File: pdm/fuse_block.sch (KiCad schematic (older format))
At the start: 15 parts, among them Q1 BC817, Q6 Q_NPN_BCE, U5 BTS443P

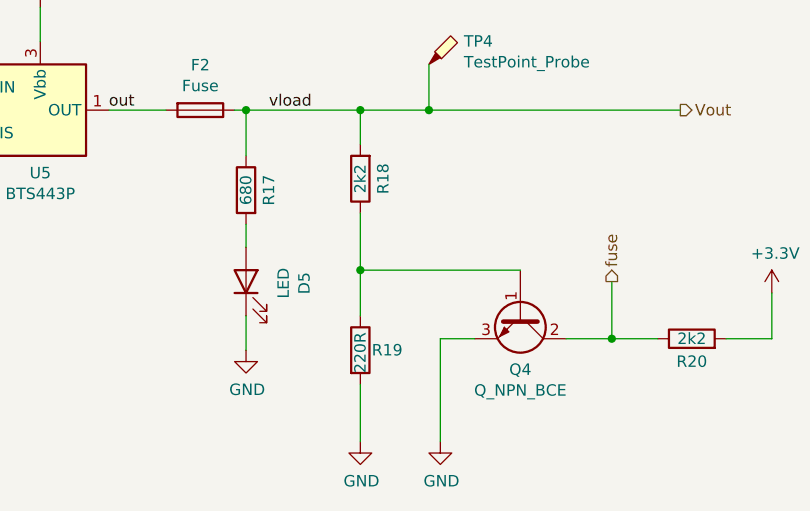
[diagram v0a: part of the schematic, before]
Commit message: added digikey BoM
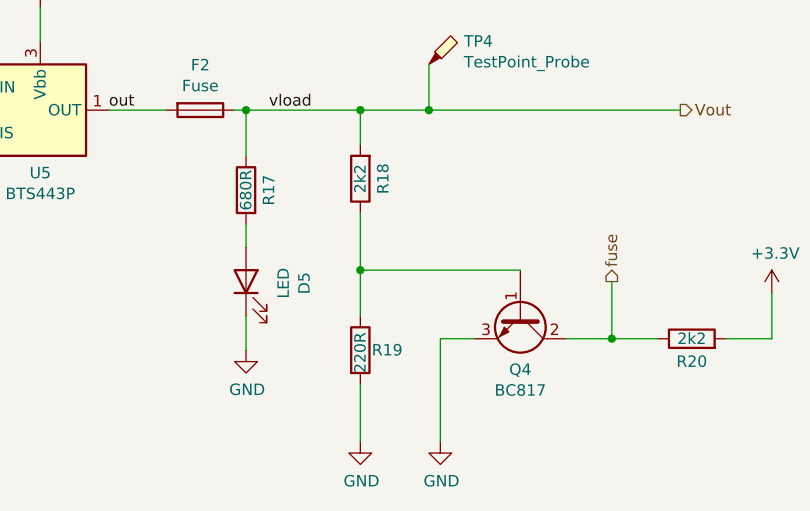
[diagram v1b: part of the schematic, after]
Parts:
- D5: Digi-Key_PN (none) -> 516-1431-1-ND
- Q1: Digi-Key_PN (none) -> 1727-6186-1-ND
- Q6: value Q_NPN_BCE -> BC817; Digi-Key_PN (none) -> 1727-6186-1-ND
- R16: Digi-Key_PN (none) -> A106057CT-ND
- R17: value 680 -> 680R; Digi-Key_PN (none) -> A129747CT-ND
- R18, R20: Digi-Key_PN (none) -> A106060CT-ND
- R19: Digi-Key_PN (none) -> 311-220CRCT-ND
- R21: Digi-Key_PN (none) -> 311-2.80KCRCT-ND
- R22: Digi-Key_PN (none) -> RNCP0805FTD10K0CT-ND
- U5: Digi-Key_PN (none) -> BTS443PAUMA1CT-ND
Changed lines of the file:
@@
 $Descr A4 11693 8268
 encoding utf-8
-Sheet 5 7
+Sheet 2 7
 Title "PDM Board"
 Date "2021-01-14"
@@
 F 2 "Package_TO_SOT_SMD:TO-252-4" H 5750 3350 50  0001 C CNN
 F 3 "http://www.infineon.com/dgdl/Infineon-BTS443P-DS-v01_00-EN.pdf?fileId=5546d4625a888733015aa9afbc5035d5" H 5750 3200 50  0001 C CNN
+F 4 "BTS443PAUMA1CT-ND" H 5750 3600 50  0001 C CNN "Digi-Key_PN"
 	1    5750 3600
 	1    0    0    -1
@@
 AR Path="/5F956034/5F954653" Ref="#PWR059"  Part="1"
 AR Path="/5F9560D2/5F954653" Ref="#PWR066"  Part="1"
-F 0 "#PWR038" H 5750 3000 50  0001 C CNN
+F 0 "#PWR052" H 5750 3000 50  0001 C CNN
 F 1 "+12V" H 5765 3323 50  0000 C CNN
 F 2 "" H 5750 3150 50  0001 C CNN
@@
 F 2 "Resistor_SMD:R_0805_2012Metric_Pad1.20x1.40mm_HandSolder" V 5080 4050 50  0001 C CNN
 F 3 "~" H 5150 4050 50  0001 C CNN
+F 4 "A106057CT-ND" H 5150 4050 50  0001 C CNN "Digi-Key_PN"
 	1    5150 4050
 	-1   0    0    1
@@
 F 2 "Resistor_SMD:R_0805_2012Metric_Pad1.20x1.40mm_HandSolder" V 7080 3900 50  0001 C CNN
 F 3 "~" H 7150 3900 50  0001 C CNN
+F 4 "A106060CT-ND" H 7150 3900 50  0001 C CNN "Digi-Key_PN"
 	1    7150 3900
 	-1   0    0    1
@@
 AR Path="/5F956034/5F954696" Ref="#PWR060"  Part="1"
 AR Path="/5F9560D2/5F954696" Ref="#PWR067"  Part="1"
-F 0 "#PWR039" H 7150 4800 50  0001 C CNN
+F 0 "#PWR053" H 7150 4800 50  0001 C CNN
 F 1 "GND" H 7155 4877 50  0000 C CNN
 F 2 "" H 7150 5050 50  0001 C CNN
@@
 Text Label 6750 3600 0    50   ~ 0
 vload
-$Comp
-L pdm-rescue:Q_NPN_BCE-Device Q6
-U 1 1 5F982D06
-P 7850 4500
-AR Path="/5F955F6E/5F982D06" Ref="Q6"  Part="1"
-AR Path="/5F9560D2/5F982D06" Ref="Q10"  Part="1"
-AR Path="/5F956034/5F982D06" Ref="Q8"  Part="1"
-AR Path="/5F94FFF3/5F982D06" Ref="Q4"  Part="1"
-AR Path="/5F955EE4/5F982D06" Ref="Q2"  Part="1"
-F 0 "Q4" V 8085 4500 50  0000 C CNN
-F 1 "Q_NPN_BCE" V 8176 4500 50  0000 C CNN
-F 2 "Package_TO_SOT_SMD:SOT-23_Handsoldering" H 8050 4600 50  0001 C CNN
-F 3 "~" H 7850 4500 50  0001 C CNN
-	1    7850 4500
-	0    1    1    0
-$EndComp
 $Comp
 L pdm-rescue:R-Device R?
@@
 F 2 "Resistor_SMD:R_0805_2012Metric_Pad1.20x1.40mm_HandSolder" V 7080 4650 50  0001 C CNN
 F 3 "~" H 7150 4650 50  0001 C CNN
+F 4 "311-220CRCT-ND" H 7150 4650 50  0001 C CNN "Digi-Key_PN"
 	1    7150 4650
 	1    0    0    -1
@@
 AR Path="/5F956034/5F98797F" Ref="#PWR062"  Part="1"
 AR Path="/5F9560D2/5F98797F" Ref="#PWR069"  Part="1"
-F 0 "#PWR041" H 8950 4250 50  0001 C CNN
+F 0 "#PWR055" H 8950 4250 50  0001 C CNN
 F 1 "+3.3V" H 8965 4573 50  0000 C CNN
 F 2 "" H 8950 4400 50  0001 C CNN
@@
 AR Path="/5F956034/5FDDFF0E" Ref="#PWR058"  Part="1"
 AR Path="/5F9560D2/5FDDFF0E" Ref="#PWR065"  Part="1"
-F 0 "#PWR037" H 5150 4050 50  0001 C CNN
+F 0 "#PWR051" H 5150 4050 50  0001 C CNN
 F 1 "GND" H 5155 4127 50  0000 C CNN
 F 2 "" H 5150 4300 50  0001 C CNN
@@
 AR Path="/5F956034/5FDE452B" Ref="#PWR057"  Part="1"
 AR Path="/5F9560D2/5FDE452B" Ref="#PWR064"  Part="1"
-F 0 "#PWR036" H 4700 4050 50  0001 C CNN
+F 0 "#PWR050" H 4700 4050 50  0001 C CNN
 F 1 "GND" H 4705 4127 50  0000 C CNN
 F 2 "" H 4700 4300 50  0001 C CNN
@@
 AR Path="/5F9560D2/5F986EB2" Ref="R38"  Part="1"
 F 0 "R17" V 6550 3950 50  0000 C CNN
-F 1 "680" V 6650 3950 50  0000 C CNN
+F 1 "680R" V 6650 3950 50  0000 C CNN
 F 2 "Resistor_SMD:R_0805_2012Metric_Pad1.20x1.40mm_HandSolder" V 6580 3950 50  0001 C CNN
 F 3 "~" H 6650 3950 50  0001 C CNN
+F 4 "A129747CT-ND" H 6650 3950 50  0001 C CNN "Digi-Key_PN"
 	1    6650 3950
 	-1   0    0    -1
@@
 F 2 "LED_SMD:LED_0805_2012Metric_Pad1.15x1.40mm_HandSolder" H 6650 4350 50  0001 C CNN
 F 3 "~" H 6650 4350 50  0001 C CNN
+F 4 "516-1431-1-ND" H 6650 4350 50  0001 C CNN "Digi-Key_PN"
 	1    6650 4350
 	0    -1   -1   0
@@
 F 2 "Resistor_SMD:R_0805_2012Metric_Pad1.20x1.40mm_HandSolder" V 8530 4600 50  0001 C CNN
 F 3 "~" H 8600 4600 50  0001 C CNN
+F 4 "A106060CT-ND" H 8600 4600 50  0001 C CNN "Digi-Key_PN"
 	1    8600 4600
 	0    -1   -1   0
@@
 AR Path="/5F956034/5FDFEAE6" Ref="#PWR061"  Part="1"
 AR Path="/5F9560D2/5FDFEAE6" Ref="#PWR068"  Part="1"
-F 0 "#PWR040" H 7500 4800 50  0001 C CNN
+F 0 "#PWR054" H 7500 4800 50  0001 C CNN
 F 1 "GND" H 7505 4877 50  0000 C CNN
 F 2 "" H 7500 5050 50  0001 C CNN
@@
 AR Path="/5F956034/6018186C" Ref="#PWR0107"  Part="1"
 AR Path="/5F9560D2/6018186C" Ref="#PWR0113"  Part="1"
-F 0 "#PWR0120" H 3200 3250 50  0001 C CNN
+F 0 "#PWR0105" H 3200 3250 50  0001 C CNN
 F 1 "GND" H 3205 3327 50  0000 C CNN
 F 2 "" H 3200 3500 50  0001 C CNN
@@
 F 2 "Resistor_SMD:R_0805_2012Metric_Pad1.20x1.40mm_HandSolder" V 4630 3500 50  0001 C CNN
 F 3 "~" H 4700 3500 50  0001 C CNN
+F 4 "RNCP0805FTD10K0CT-ND" H 4700 3500 50  0001 C CNN "Digi-Key_PN"
 	1    4700 3500
 	0    -1   -1   0
@@
 F 2 "Resistor_SMD:R_0805_2012Metric_Pad1.20x1.40mm_HandSolder" V 3830 3050 50  0001 C CNN
 F 3 "~" H 3900 3050 50  0001 C CNN
+F 4 "311-2.80KCRCT-ND" H 3900 3050 50  0001 C CNN "Digi-Key_PN"
 	1    3900 3050
 	1    0    0    -1
@@
 F 2 "Package_TO_SOT_SMD:SOT-23" H 4100 3325 50  0001 L CIN
 F 3 "https://www.onsemi.com/pub/Collateral/BC818-D.pdf" H 3900 3400 50  0001 L CNN
+F 4 "1727-6186-1-ND" H 3900 3400 50  0001 C CNN "Digi-Key_PN"
 	1    3900 3400
 	0    1    1    0
@@
 AR Path="/5F956034/60198289" Ref="#PWR0112"  Part="1"
 AR Path="/5F9560D2/60198289" Ref="#PWR0114"  Part="1"
-F 0 "#PWR0121" H 6650 4400 50  0001 C CNN
+F 0 "#PWR0106" H 6650 4400 50  0001 C CNN
 F 1 "GND" H 6655 4477 50  0000 C CNN
 F 2 "" H 6650 4650 50  0001 C CNN
@@
 Wire Wire Line
 	6650 3600 7150 3600
+$Comp
+L pdm-rescue:Q_NPN_BCE-Device Q6
+U 1 1 5F982D06
+P 7850 4500
+AR Path="/5F955F6E/5F982D06" Ref="Q6"  Part="1"
+AR Path="/5F9560D2/5F982D06" Ref="Q10"  Part="1"
+AR Path="/5F956034/5F982D06" Ref="Q8"  Part="1"
+AR Path="/5F94FFF3/5F982D06" Ref="Q4"  Part="1"
+AR Path="/5F955EE4/5F982D06" Ref="Q2"  Part="1"
+F 0 "Q4" V 8085 4500 50  0000 C CNN
+F 1 "BC817" V 8176 4500 50  0000 C CNN
+F 2 "Package_TO_SOT_SMD:SOT-23_Handsoldering" H 8050 4600 50  0001 C CNN
+F 3 "~" H 7850 4500 50  0001 C CNN
+F 4 "1727-6186-1-ND" H 7850 4500 50  0001 C CNN "Digi-Key_PN"
+	1    7850 4500
+	0    1    1    0
+$EndComp
 $EndSCHEMATC

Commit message: added fixes for issue #11 #12 & #13
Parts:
- added Q12: BC817, Package_TO_SOT_SMD:SOT-23, symbol pdm-rescue:Q_NPN_BCE-Device
- added R45: 10k, Resistor_SMD:R_0805_2012Metric_Pad1.20x1.40mm_HandSolder, symbol pdm-rescue:R-Device
- C13: Digi-Key_PN T494A106M020AT -> 1276-6471-1-ND
- Q6: footprint Package_TO_SOT_SMD:SOT-23_Handsoldering -> Package_TO_SOT_SMD:SOT-23
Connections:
- wire segments 36 -> 39
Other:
- note removed: "make sure led can handle appropriate back voltage"
- moved on the sheet: D6, R24

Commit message: Fixed LED Work
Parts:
- C13: Mouser PN (none) -> 603-CC0805MKX58BB105
- D5: Mouser PN (none) -> 630-HSMR-C170-R0000
- Q1, Q12, Q6: Mouser PN (none) -> 771-BC817K-40HVL
- R16: Mouser PN (none) -> 603-RT0805FRE101K5L
- R18, R20: Mouser PN (none) -> RT0805FRE072K2L
- R19: Mouser PN (none) -> 603-RT0805FRE10220RL
- R21: value 2k8 -> 2k2; Mouser PN (none) -> RT0805FRE072K2L
- R22: Mouser PN (none) -> 603-AC0805FR-0710K5L
- R31: renamed from R17; value 680R -> 850; Mouser PN (none) -> 667-ERJ-6ENF8660V
- R45: value 10k -> 2k2; Mouser PN (none) -> RT0805FRE072K2L
- U5: Mouser PN (none) -> 726-BTS443P
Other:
- moved on the sheet: D7, Q13, R31, R43

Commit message: changed oscilltor and exposed themral pads
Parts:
- renumbered C13 to C11, D5 to D6, F2 to F4, Q12 to Q2, Q6 to Q3, R21 to R29, R22 to R30, R16 to R31, R31 to R32, R18 to R33, R19 to R34, R45 to R35, R20 to R36, TP5 to TP1, U5 to U6, TP6 to Vout_TP1

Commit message: major redesign - hc switching output
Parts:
- removed Q1: BC817, Package_TO_SOT_SMD:SOT-23, symbol Transistor_BJT:BC817
- removed Q3: BC817, Package_TO_SOT_SMD:SOT-23, symbol pdm-rescue:Q_NPN_BCE-Device
- removed R33, R36: 2k2, Resistor_SMD:R_0805_2012Metric_Pad1.20x1.40mm_HandSolder, symbol pdm-rescue:R-Device
- removed R34: 220R, Resistor_SMD:R_0805_2012Metric_Pad1.20x1.40mm_HandSolder, symbol pdm-rescue:R-Device
- added 10k?: R, symbol Device:R
- added Q? (x2): Q_NMOS_DGS, symbol Device:Q_NMOS_DGS
- added R?: 10k, symbol Device:R
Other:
- note added: "Fuse Detect"

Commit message: fixed schematic
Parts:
- removed Q2: BC817, Package_TO_SOT_SMD:SOT-23, symbol pdm-rescue:Q_NPN_BCE-Device
- removed Q? (x2): Q_NMOS_DGS, symbol Device:Q_NMOS_DGS
- removed R29, R35: 2k2, Resistor_SMD:R_0805_2012Metric_Pad1.20x1.40mm_HandSolder, symbol pdm-rescue:R-Device
- removed TP1, Vout_TP1: TestPoint_Probe, TestPoint:TestPoint_Pad_D1.0mm, symbol pdm-rescue:TestPoint_Probe-Connector
- added 10k6, 10k?: R, Resistor_SMD:R_0603_1608Metric, symbol Device:R
- added C25: 10uF, Capacitor_SMD:C_0603_1608Metric, symbol Device:C
- added Q? (x3): 2N7000, Package_TO_SOT_THT:TO-92_Inline, symbol Transistor_FET:2N7000
- added R12, R13: NC, Resistor_SMD:R_0603_1608Metric, symbol Device:R
- 10k5: renamed from 10k?; footprint (none) -> Resistor_SMD:R_0603_1608Metric
- C13: renamed from C11; footprint Capacitor_SMD:C_0805_2012Metric_Pad1.18x1.45mm_HandSolder -> Capacitor_SMD:C_0603_1608Metric
- F2: renamed from F4; footprint pdm_v2:fuseHolder -> Fuse:Fuse_1206_3216Metric
- R14: renamed from R?; footprint (none) -> Resistor_SMD:R_0603_1608Metric
- renumbered D6 to D4, R31 to R10, R32 to R11, R30 to R9, U6 to U5
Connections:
- wire segments 39 -> 46
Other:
- note added: "ADC Sense"
- note added: "Indicator LED"
- note added: "Place near MCU"
- note added: "added cap to get rid of pwm bad signals\nthere may be some delay but it seems okay?"
- note removed: "Fuse Detect"
- moved on the sheet: 10k1, D3, R5, R8

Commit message: new layout
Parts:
- removed C25: 10uF, Capacitor_SMD:C_0603_1608Metric, symbol Device:C
- removed Q? (x3): 2N7000, Package_TO_SOT_THT:TO-92_Inline, symbol Transistor_FET:2N7000
- removed R12, R13: NC, Resistor_SMD:R_0603_1608Metric, symbol Device:R
- added Q12, Q13, Q14: 2N7002E, Package_TO_SOT_SMD:SOT-23, symbol Transistor_FET:2N7002E
- D4: footprint LED_SMD:LED_0805_2012Metric_Pad1.15x1.40mm_HandSolder -> LED_SMD:LED_0603_1608Metric
- R13: renamed from R9; footprint Resistor_SMD:R_0805_2012Metric_Pad1.20x1.40mm_HandSolder -> Resistor_SMD:R_0603_1608Metric
- R14: renamed from R10; footprint Resistor_SMD:R_0805_2012Metric_Pad1.20x1.40mm_HandSolder -> Resistor_SMD:R_0603_1608Metric
- R15: renamed from R11; footprint Resistor_SMD:R_0805_2012Metric_Pad1.20x1.40mm_HandSolder -> Resistor_SMD:R_0603_1608Metric
- R21: renamed from 10k5; value R -> 10k
- R25: renamed from 10k6; value R -> 10k
- R29: renamed from 10k?; value R -> 10k
- renumbered R14 to R19
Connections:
- net GND: now also Q12.2 (S), Q13.2 (S), Q14.2 (S)
- net Vout: now also R19.1, Q14.1 (G)
- net activate: now also Q12.1 (G), Q13.1 (G)
- net at D4.1 (K): now also Q13.3 (D)
- net at R13.1: now also Q12.3 (D)
- net fuse: now reaches R29.2
- net fuse: now also Q14.3 (D)
- net out renamed out-unfused
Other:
- moved on the sheet: C24, F5, R39, R40

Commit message: adding BoM
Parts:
- C13: Digi-Key_PN 1276-6471-1-ND -> 1276-1859-2-ND
- D4: Digi-Key_PN 516-1431-1-ND -> 516-3541-1-ND
- F2: Digi-Key_PN (none) -> 486-1688-2-ND
- Q12, Q13, Q14: Digi-Key_PN (none) -> 2N7002E-FDICT-ND
- R14: Digi-Key_PN A106057CT-ND -> P1.50KHTR-ND
- R15: Digi-Key_PN A129747CT-ND -> 311-845HRCT-ND
- R19, R21, R25, R29: Digi-Key_PN (none) -> RNCP0805FTD10K0CT-ND
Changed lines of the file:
@@
 F 2 "Resistor_SMD:R_0603_1608Metric" V 7080 3250 50  0001 C CNN
 F 3 "~" H 7150 3250 50  0001 C CNN
-F 4 "A129747CT-ND" H 7150 3250 50  0001 C CNN "Digi-Key_PN"
+F 4 "311-845HRCT-ND" H 7150 3250 50  0001 C CNN "Digi-Key_PN"
 F 5 "667-ERJ-6ENF8660V" H 7150 3250 50  0001 C CNN "Mouser PN"
 	1    7150 3250
@@
 F 2 "LED_SMD:LED_0603_1608Metric" H 7150 2850 50  0001 C CNN
 F 3 "~" H 7150 2850 50  0001 C CNN
-F 4 "516-1431-1-ND" H 7150 2850 50  0001 C CNN "Digi-Key_PN"
+F 4 "516-3541-1-ND" H 7150 2850 50  0001 C CNN "Digi-Key_PN"
 F 5 "630-HSMR-C170-R0000" H 7150 2850 50  0001 C CNN "Mouser PN"
 	1    7150 2850
@@
 F 2 "Capacitor_SMD:C_0603_1608Metric" H 4588 3900 50  0001 C CNN
 F 3 "~" H 4550 4050 50  0001 C CNN
-F 4 "1276-6471-1-ND" H 4550 4050 50  0001 C CNN "Digi-Key_PN"
+F 4 "1276-1859-2-ND" H 4550 4050 50  0001 C CNN "Digi-Key_PN"
 F 5 "603-CC0805MKX58BB105" H 4550 4050 50  0001 C CNN "Mouser PN"
 	1    4550 4050
@@
 F 2 "Fuse:Fuse_1206_3216Metric" V 6580 3600 50  0001 C CNN
 F 3 "~" H 6650 3600 50  0001 C CNN
+F 4 "486-1688-2-ND" H 6650 3600 50  0001 C CNN "Digi-Key_PN"
 	1    6650 3600
 	0    1    1    0
@@
 F 2 "Resistor_SMD:R_0603_1608Metric" V 4930 4050 50  0001 C CNN
 F 3 "~" H 5000 4050 50  0001 C CNN
-F 4 "A106057CT-ND" H 5000 4050 50  0001 C CNN "Digi-Key_PN"
+F 4 "P1.50KHTR-ND" H 5000 4050 50  0001 C CNN "Digi-Key_PN"
 F 5 "603-RT0805FRE101K5L" H 5000 4050 50  0001 C CNN "Mouser PN"
 	1    5000 4050
@@
 F 2 "Resistor_SMD:R_0603_1608Metric" V 8380 5200 50  0001 C CNN
 F 3 "~" H 8450 5200 50  0001 C CNN
+F 4 "RNCP0805FTD10K0CT-ND" H 8450 5200 50  0001 C CNN "Digi-Key_PN"
 	1    8450 5200
 	1    0    0    -1
@@
 F 2 "Resistor_SMD:R_0603_1608Metric" V 3380 2600 50  0001 C CNN
 F 3 "~" H 3450 2600 50  0001 C CNN
+F 4 "RNCP0805FTD10K0CT-ND" H 3450 2600 50  0001 C CNN "Digi-Key_PN"
 	1    3450 2600
 	1    0    0    -1
@@
 F 2 "Resistor_SMD:R_0603_1608Metric" V 7530 2750 50  0001 C CNN
 F 3 "~" H 7600 2750 50  0001 C CNN
+F 4 "RNCP0805FTD10K0CT-ND" H 7600 2750 50  0001 C CNN "Digi-Key_PN"
 	1    7600 2750
 	1    0    0    -1
@@
 F 2 "Resistor_SMD:R_0603_1608Metric" V 8780 4450 50  0001 C CNN
 F 3 "~" H 8850 4450 50  0001 C CNN
+F 4 "RNCP0805FTD10K0CT-ND" H 8850 4450 50  0001 C CNN "Digi-Key_PN"
 	1    8850 4450
 	1    0    0    -1
@@
 F 2 "Package_TO_SOT_SMD:SOT-23" H 8950 4825 50  0001 L CIN
 F 3 "http://www.diodes.com/assets/Datasheets/ds30376.pdf" H 8750 4900 50  0001 L CNN
+F 4 "2N7002E-FDICT-ND" H 8750 4900 50  0001 C CNN "Digi-Key_PN"
 	1    8750 4900
 	1    0    0    -1
@@
 F 2 "Package_TO_SOT_SMD:SOT-23" H 7450 2375 50  0001 L CIN
 F 3 "http://www.diodes.com/assets/Datasheets/ds30376.pdf" H 7250 2450 50  0001 L CNN
+F 4 "2N7002E-FDICT-ND" H 7250 2450 50  0001 C CNN "Digi-Key_PN"
 	1    7250 2450
 	-1   0    0    1
@@
 F 2 "Package_TO_SOT_SMD:SOT-23" H 4100 3325 50  0001 L CIN
 F 3 "http://www.diodes.com/assets/Datasheets/ds30376.pdf" H 3900 3400 50  0001 L CNN
+F 4 "2N7002E-FDICT-ND" H 3900 3400 50  0001 C CNN "Digi-Key_PN"
 	1    3900 3400
 	0    1    1    0
